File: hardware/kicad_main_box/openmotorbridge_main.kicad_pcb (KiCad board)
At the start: 4 copper layers, 85 x 55 mm, 40 parts, among them J1 IDC_2X13_HEADER, J2 MicroSD_4Bit_SDIO, J3 USB_C_IP67, J4 LED_EXT, J5 BAT_LIPO_3V7, J6 NTC_10K_JEITA, T1 Bourns_LM-NP-1001_Audio1, T2 Bourns_LM-NP-1001_Audio2, U1 LM5164-Q1, U2 ESP32-S3-WROOM-1, U3 ES8388, U4 B0505S-1WR3, U5 BMI270, U6 TCAN334G, U7 TLP222A_Opto1, U8 TLP222A_Opto2, U9 TPS7A0533_LDO

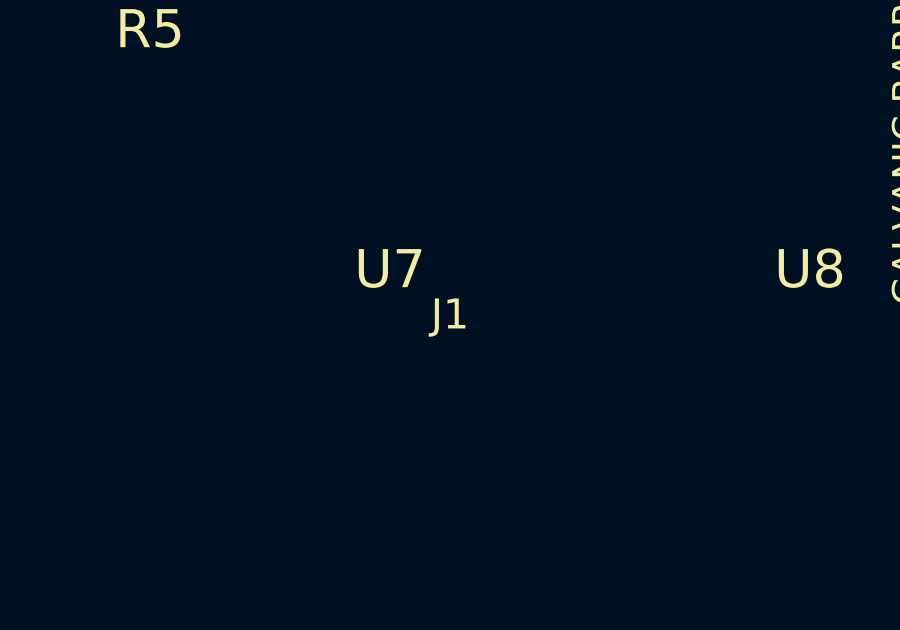
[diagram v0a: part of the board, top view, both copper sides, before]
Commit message: fix(kicad): set J1 footprint rotation to 90.0 deg so IDC-Header 2x13 3D model is parallel to long edge in KiCad 3D viewer
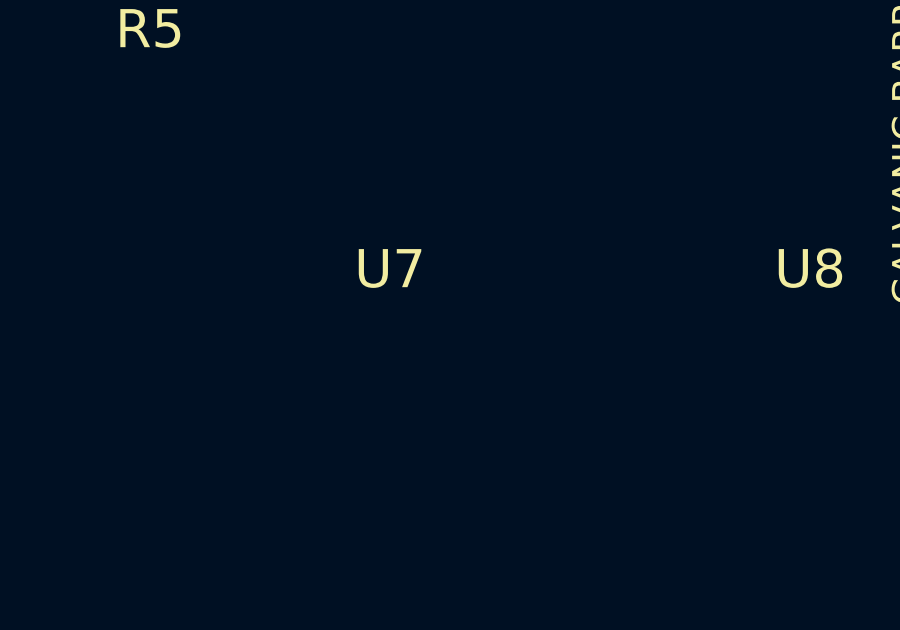
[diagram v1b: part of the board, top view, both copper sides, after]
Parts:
- ?: renamed from J1; footprint Connector_Dsub:DSUB-26-HD_Female_Horizontal_P2.29x1.98mm_EdgePinOffset7.70mm_Housings_POS01 -> Connector_IDC:IDC-Header_2x13_P2.54mm_Vertical
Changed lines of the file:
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@@
 		)
 	)
-	(footprint "Connector_Dsub:DSUB-26-HD_Female_Horizontal_P2.29x1.98mm_EdgePinOffset7.70mm_Housings_POS01"
+	(footprint "Connector_IDC:IDC-Header_2x13_P2.54mm_Vertical"
 		(layer "F.Cu")
-		(at 168.00 118.50)
-		(property "Reference" "J1"
+		(at 168.00 118.50 90.0118.50
 			(at 0 -12 180)
 			(layer "F.SilkS")

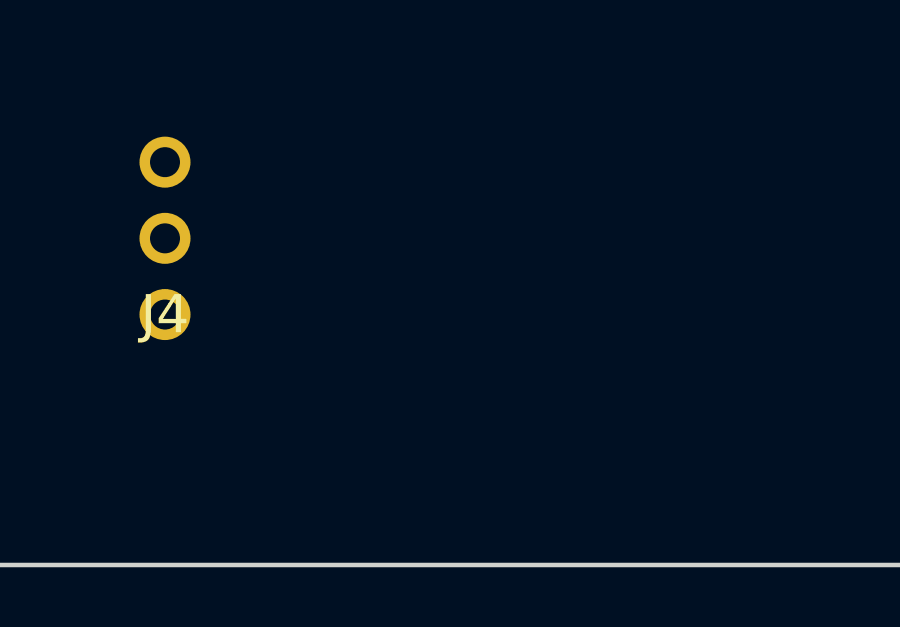
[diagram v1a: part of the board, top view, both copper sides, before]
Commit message: fix(kicad): resolve parenthesis syntax error on J1 footprint line 1853
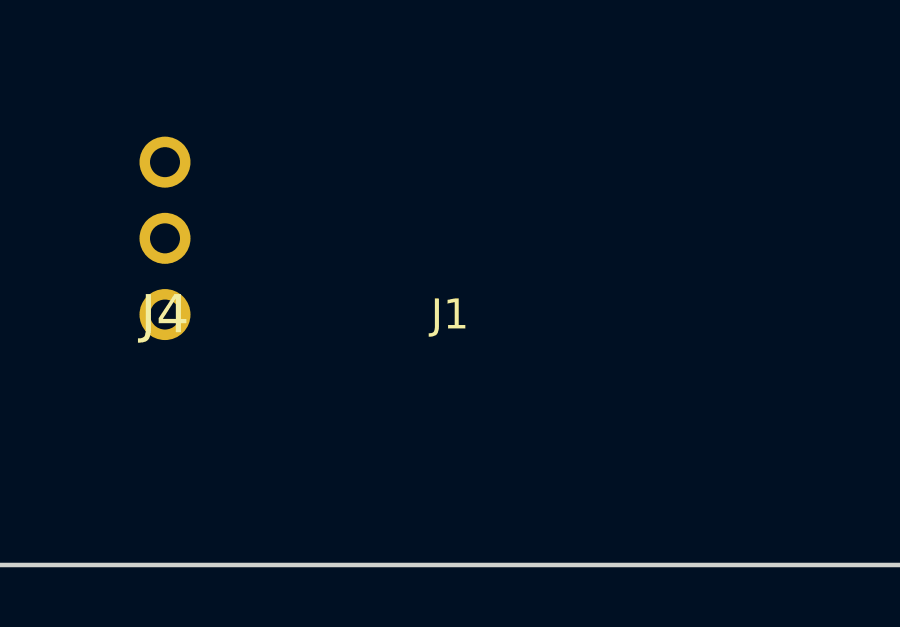
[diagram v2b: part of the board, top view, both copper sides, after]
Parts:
- turned J1 to 90 degrees
- gave numbers to parts that had none: 1
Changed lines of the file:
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@@
 	(footprint "Connector_IDC:IDC-Header_2x13_P2.54mm_Vertical"
 		(layer "F.Cu")
-		(at 168.00 118.50 90.0118.50
+		(at 168.00 118.50 90.0)
+		(property "Reference" "J1"
 			(at 0 -12 180)
 			(layer "F.SilkS")

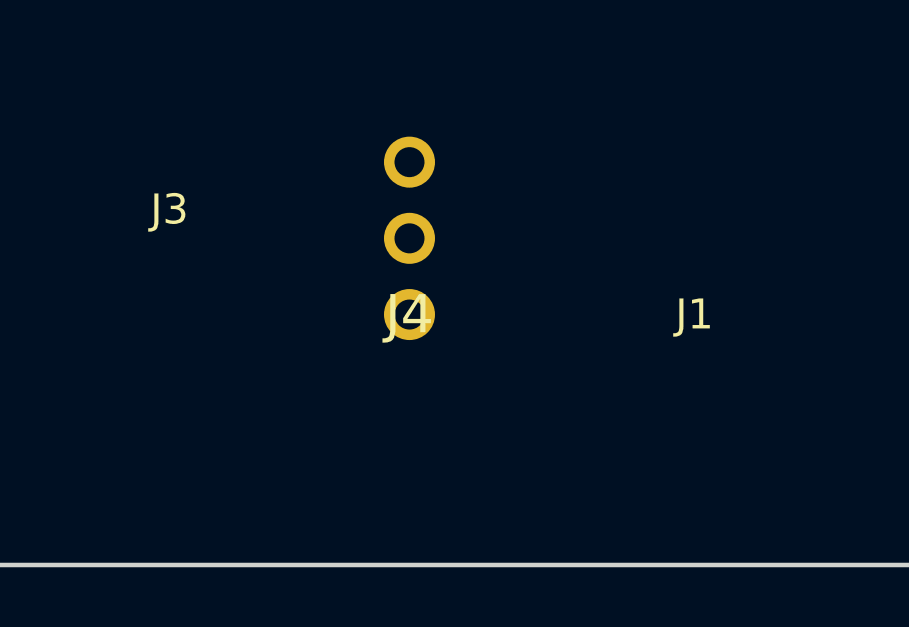
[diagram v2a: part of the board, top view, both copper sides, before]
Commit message: fix(kicad): shift J1 footprint origin to X=152.0 to account for KiCad Pin 1 footprint anchor
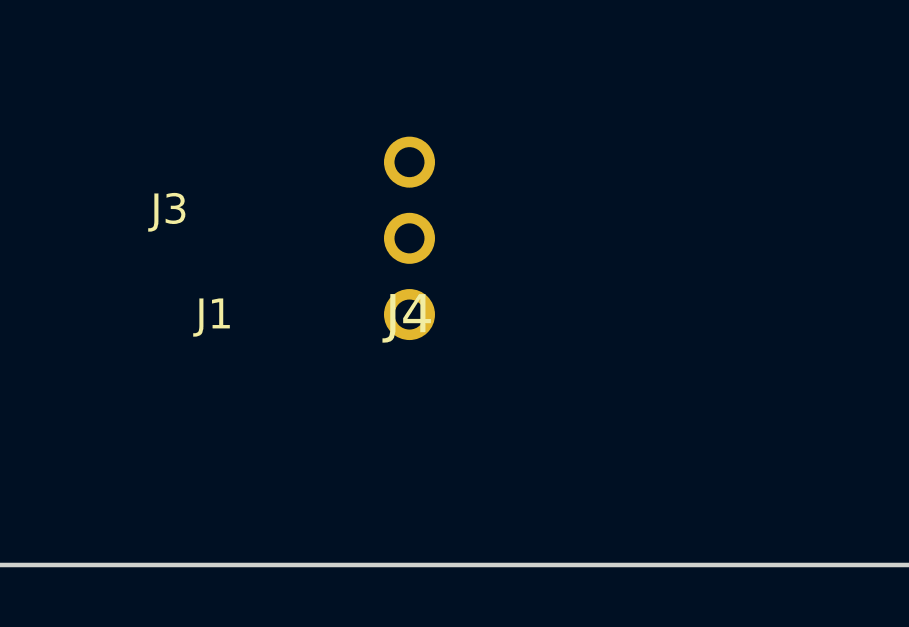
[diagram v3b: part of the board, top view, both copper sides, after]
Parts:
- moved J1 16.0 mm to (152.0, 118.5)
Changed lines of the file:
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@@
 	(footprint "Connector_IDC:IDC-Header_2x13_P2.54mm_Vertical"
 		(layer "F.Cu")
-		(at 168.00 118.50 90.0)
+		(at 152.00 118.50 90.0)
 		(property "Reference" "J1"
 			(at 0 -12 180)

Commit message: fix(pcb): rotate J4 vertically in Y and compact left connectors to ensure 4.5mm air gap to J1
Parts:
- moved J4 146.5 mm to (0.00, 116.0), turned to 0 degrees
- moved J3 138.5 mm to (0.00, 118.5), turned to 90 degrees
- moved J6 131.0 mm to (0.00, 117.0), turned to 0 degrees
- moved J5 125.5 mm to (0.00, 118.5), turned to 0 degrees
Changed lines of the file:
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@@
 	(footprint ""
 		(layer "F.Cu")
-		(at 131.00 118.50 90.0)
+		(at Connector_PinHeader_2.54mm:PinHeader_1x02_P2.54mm_Vertical131.00132.50 117.00)
 		(property "Reference" "J6"
 			(at 0 0 0)
@@
 	(footprint "Connector_USB:USB_C_Receptacle_GCT_USB4085"
 		(layer "F.Cu")
-		(at 138.50 118.50)
+		(at Connector_USB:USB_C_Receptacle_GCT_USB4105-xx_Vertical138.50139.00 118.50 90.0)
 		(property "Reference" "J3"
 			(at 0 -3.5 0)
@@
 	(footprint ""
 		(layer "F.Cu")
-		(at 146.50 118.50 90.0)
+		(at Connector_PinHeader_2.54mm:PinHeader_1x03_P2.54mm_Vertical146.50145.50 116.00)
 		(property "Reference" "J4"
 			(at 0 0 0)
@@
 	(footprint ""
 		(layer "F.Cu")
-		(at 125.50 118.50 90.0)
+		(at Connector_JST:JST_PH_S2B-PH-K_1x02_P2.00mm_Horizontal125.50126.50 118.50)
 		(property "Reference" "J5"
 			(at 0 0 0)

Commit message: fix(kicad): clean up all malformed footprint coordinate lines in openmotorbridge_main.kicad_pcb
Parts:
- J4: footprint (none) -> Connector_PinHeader_2.54mm:PinHeader_1x03_P2.54mm_Vertical
- J6: footprint (none) -> Connector_PinHeader_2.54mm:PinHeader_1x02_P2.54mm_Vertical
- moved J4 145.5 mm to (145.5, 116.0)
- moved J3 139.0 mm to (139.0, 118.5)
- moved J6 132.5 mm to (132.5, 117.0)
- moved J5 126.5 mm to (126.5, 118.5)
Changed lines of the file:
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@@
 		)
 	)
-	(footprint ""
-		(layer "F.Cu")
-		(at Connector_PinHeader_2.54mm:PinHeader_1x02_P2.54mm_Vertical131.00132.50 117.00)
+	(footprint "Connector_PinHeader_2.54mm:PinHeader_1x02_P2.54mm_Vertical"
+		(layer "F.Cu")
+		(at 132.50 117.00)
 		(property "Reference" "J6"
 			(at 0 0 0)
@@
 	(footprint "Connector_USB:USB_C_Receptacle_GCT_USB4085"
 		(layer "F.Cu")
-		(at Connector_USB:USB_C_Receptacle_GCT_USB4105-xx_Vertical138.50139.00 118.50 90.0)
+		(at 139.00 118.50 90.0)
 		(property "Reference" "J3"
 			(at 0 -3.5 0)
@@
 		)
 	)
-	(footprint ""
-		(layer "F.Cu")
-		(at Connector_PinHeader_2.54mm:PinHeader_1x03_P2.54mm_Vertical146.50145.50 116.00)
+	(footprint "Connector_PinHeader_2.54mm:PinHeader_1x03_P2.54mm_Vertical"
+		(layer "F.Cu")
+		(at 145.50 116.00)
 		(property "Reference" "J4"
 			(at 0 0 0)
@@
 	(footprint ""
 		(layer "F.Cu")
-		(at Connector_JST:JST_PH_S2B-PH-K_1x02_P2.00mm_Horizontal125.50126.50 118.50)
+		(at 126.50 118.50)
 		(property "Reference" "J5"
 			(at 0 0 0)

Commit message: feat(pcb): move J5 battery connector to short left edge and space J6, J3, J4, J1 with >3.2mm air gaps
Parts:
- moved J6 5.22 mm to (127.5, 118.5)
- moved J4 1.50 mm to (144.0, 116.0)
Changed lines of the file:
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@@
 	(footprint "Connector_PinHeader_2.54mm:PinHeader_1x02_P2.54mm_Vertical"
 		(layer "F.Cu")
-		(at 132.50 117.00)
+		(at 127.50 118.50)
 		(property "Reference" "J6"
 			(at 0 0 0)
@@
 	(footprint "Connector_PinHeader_2.54mm:PinHeader_1x03_P2.54mm_Vertical"
 		(layer "F.Cu")
-		(at 145.50 116.00)
+		(at 144.00 116.00)
 		(property "Reference" "J4"
 			(at 0 0 0)

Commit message: feat(power): unify battery and NTC into single 4-pin JST-PH shrouded connector (J5) on short left PCB flank
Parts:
- removed J6: NTC_10K_JEITA, Connector_PinHeader_2.54mm:PinHeader_1x02_P2.54mm_Vertical
- moved J4 0.50 mm to (143.5, 116.0)
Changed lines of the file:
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@@
-		)
-	)
-	(footprint "Connector_PinHeader_2.54mm:PinHeader_1x02_P2.54mm_Vertical"
-		(layer "F.Cu")
-		(at 127.50 118.50)
-		(property "Reference" "J6"
-			(at 0 0 0)
-			(layer "F.SilkS")
-			(effects
-				(font
-					(size 1.27 1.27)
-				)
-			)
-		)
-		(property "Value" "NTC_10K_JEITA"
-			(at 0 0 0)
-			(layer "F.Fab")
-			(effects
-				(font
-					(size 1.27 1.27)
-				)
-			)
-		)
-		(property "Datasheet" ""
-			(at 0 0 0)
-			(layer "F.Fab")
-			(hide yes)
-			(effects
-				(font
-					(size 1.27 1.27)
-				)
-			)
-		)
-		(property "Description" ""
-			(at 0 0 0)
-			(layer "F.Fab")
-			(hide yes)
-			(effects
-				(font
-					(size 1.27 1.27)
-				)
-			)
-		)
-		(duplicate_pad_numbers_are_jumpers no)
-		(pad "1" thru_hole circle
-			(at 0 0)
-			(size 1.7 1.7)
-			(drill 1)
-			(layers "*.Cu")
-			(remove_unused_layers no)
-		)
-		(pad "2" thru_hole circle
-			(at 2.54 0)
-			(size 1.7 1.7)
-			(drill 1)
-			(layers "*.Cu")
-			(remove_unused_layers no)
-		)
-		(embedded_fonts no)
-		(model "${KICAD10_3DMODEL_DIR}/Connector_PinHeader_2.54mm.3dshapes/PinHeader_1x02_P2.54mm_Vertical.step"
-			(offset
-				(xyz 0 0 0)
-			)
-			(scale
-				(xyz 1 1 1)
-			)
-			(rotate
-				(xyz 0 0 0)
-			)
 		)
 	)
@@
 	(footprint "Connector_PinHeader_2.54mm:PinHeader_1x03_P2.54mm_Vertical"
 		(layer "F.Cu")
-		(at 144.00 116.00)
+		(at 143.50 116.00)
 		(property "Reference" "J4"
 			(at 0 0 0)

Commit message: fix(kicad): update J5 3D model link to official 4-pin JST_PH_B4B-PH-K_1x04_P2.00mm_Vertical.step
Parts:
- J5: value BAT_LIPO_3V7 -> JST_PH_4P_BAT_NTC; footprint (none) -> Connector_JST:JST_PH_B4B-PH-K_1x04_P2.00mm_Vertical
- moved J5 8.85 mm to (120.0, 112.5), turned to 90 degrees
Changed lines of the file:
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@@
 		(embedded_fonts no)
 	)
-	(footprint ""
+	(footprint "Connector_JST:JST_PH_B4B-PH-K_1x04_P2.00mm_Vertical"
 		(layer "F.Cu")
-		(at 126.50 118.50)
+		(at 120.00 112.50 90.0)
 		(property "Reference" "J5"
-			(at 0 0 0)
+			(at 0 -2.5 90)
 			(layer "F.SilkS")
 			(effects
 				(font
-					(size 1.27 1.27)
+					(size 1 1)
+					(thickness 0.15)
 				)
 			)
 		)
-		(property "Value" "BAT_LIPO_3V7"
-			(at 0 0 0)
+		(property "Value" "JST_PH_4P_BAT_NTC"
+			(at 3 4.5 90)
 			(layer "F.Fab")
 			(effects
 				(font
-					(size 1.27 1.27)
+					(size 1 1)
+					(thickness 0.15)
 				)
 			)
 		)
-		(property "Datasheet" ""
+		(property "Datasheet" "https://www.jst-mfg.com/product/pdf/eng/ePH.pdf"
 			(at 0 0 0)
 			(layer "F.Fab")
 			(hide yes)
-			(effects
-				(font
-					(size 1.27 1.27)
-				)
-			)
 		)
-		(property "Description" ""
+		(property "Description" "JST PH series connector, 4-pin vertical shrouded header (BAT+, BAT-, NTC, GND)"
 			(at 0 0 0)
 			(layer "F.Fab")
 			(hide yes)
-			(effects
-				(font
-					(size 1.27 1.27)
-				)
-			)
 		)
-		(duplicate_pad_numbers_are_jumpers no)
-		(pad "1" thru_hole circle
-			(at 0 0)
+		(fp_line
+			(start -2.0 -2.25)
+			(end 8.0 -2.25)
+			(stroke (width 0.15) (type solid))
+			(layer "F.SilkS")
+		)
+		(fp_line
+			(start 8.0 -2.25)
+			(end 8.0 2.25)
+			(stroke (width 0.15) (type solid))
+			(layer "F.SilkS")
+		)
+		(fp_line
+			(start 8.0 2.25)
+			(end -2.0 2.25)
+			(stroke (width 0.15) (type solid))
+			(layer "F.SilkS")
+		)
+		(fp_line
+			(start -2.0 2.25)
+			(end -2.0 -2.25)
+			(stroke (width 0.15) (type solid))
+			(layer "F.SilkS")
+		)
+		(pad "1" thru_hole rect
+			(at 0 0 90)
 			(size 1.7 1.7)
-			(drill 1)
-			(layers "*.Cu")
+			(drill 0.8)
+			(layers "*.Cu" "*.Mask")
 			(remove_unused_layers no)
 		)
 		(pad "2" thru_hole circle
-			(at 2.54 0)
+			(at 2.0 0 90)
 			(size 1.7 1.7)
-			(drill 1)
-			(layers "*.Cu")
+			(drill 0.8)
+			(layers "*.Cu" "*.Mask")
+			(remove_unused_layers no)
+		)
+		(pad "3" thru_hole circle
+			(at 4.0 0 90)
+			(size 1.7 1.7)
+			(drill 0.8)
+			(layers "*.Cu" "*.Mask")
+			(remove_unused_layers no)
+		)
+		(pad "4" thru_hole circle
+			(at 6.0 0 90)
+			(size 1.7 1.7)
+			(drill 0.8)
+			(layers "*.Cu" "*.Mask")
 			(remove_unused_layers no)
 		)
 		(embedded_fonts no)
-		(model "${KICAD10_3DMODEL_DIR}/Connector_JST.3dshapes/JST_PH_B2B-PH-K_1x02_P2.00mm_Vertical.step"
+		(model "${KICAD10_3DMODEL_DIR}/Connector_JST.3dshapes/JST_PH_B4B-PH-K_1x04_P2.00mm_Vertical.step"
 			(offset
-				(xyz 0 0 0)
+				(xyz 3 0 0)
 			)
 			(scale
